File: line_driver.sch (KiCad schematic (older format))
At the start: 30 parts, among them J7 DRV632

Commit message: Add LEDs to MCU and polarized caps on line driver.
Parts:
- removed C12, C16, C19, C8: 1uF, symbol C
- added C12, C16, C19, C8: 1uF, symbol CP
- renumbered R7 to R10, R8 to R11, R9 to R12, R10 to R13, R11 to R14, R12 to R15, R13 to R16, R14 to R17, R15 to R18, R16 to R19, R17 to R20, R4 to R7, R5 to R8, R6 to R9
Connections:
- net L+: now also C19.1
- net L-: now also C16.1
- net R+: now also C12.1
- net R-: now also C8.1
- net at R15.1: now also C16.2
- net at R11.1: now also C12.2
- net at R17.1: now also C19.2
- net at R9.1: now also C8.2
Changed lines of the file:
@@
 $EndDescr
 $Comp
-L GND #PWR023
+L GND #PWR25
 U 1 1 59178E76
 P 4800 3400
-F 0 "#PWR023" H 4800 3150 50  0001 C CNN
+F 0 "#PWR25" H 4800 3150 50  0001 C CNN
 F 1 "GND" H 4800 3250 50  0000 C CNN
 F 2 "" H 4800 3400 50  0001 C CNN
@@
 $EndComp
 $Comp
-L GND #PWR024
+L GND #PWR31
 U 1 1 59178E8C
 P 6800 3500
-F 0 "#PWR024" H 6800 3250 50  0001 C CNN
+F 0 "#PWR31" H 6800 3250 50  0001 C CNN
 F 1 "GND" H 6800 3350 50  0000 C CNN
 F 2 "" H 6800 3500 50  0001 C CNN
@@
 $EndComp
 $Comp
-L GND #PWR025
+L GND #PWR27
 U 1 1 59178F5E
 P 5150 4050
-F 0 "#PWR025" H 5150 3800 50  0001 C CNN
+F 0 "#PWR27" H 5150 3800 50  0001 C CNN
 F 1 "GND" H 5150 3900 50  0000 C CNN
 F 2 "" H 5150 4050 50  0001 C CNN
@@
 $EndComp
 $Comp
-L GND #PWR026
+L GND #PWR29
 U 1 1 59178FEA
 P 6450 4050
-F 0 "#PWR026" H 6450 3800 50  0001 C CNN
+F 0 "#PWR29" H 6450 3800 50  0001 C CNN
 F 1 "GND" H 6450 3900 50  0000 C CNN
 F 2 "" H 6450 4050 50  0001 C CNN
@@
 	6450 3950 6450 4050
 $Comp
-L VCC #PWR027
+L VCC #PWR30
 U 1 1 59179027
 P 6650 3650
-F 0 "#PWR027" H 6650 3500 50  0001 C CNN
+F 0 "#PWR30" H 6650 3500 50  0001 C CNN
 F 1 "VCC" H 6650 3800 50  0000 C CNN
 F 2 "" H 6650 3650 50  0001 C CNN
@@
 Connection ~ 6450 3600
 $Comp
-L VCC #PWR028
+L VCC #PWR26
 U 1 1 59179085
 P 4950 3500
-F 0 "#PWR028" H 4950 3350 50  0001 C CNN
+F 0 "#PWR26" H 4950 3350 50  0001 C CNN
 F 1 "VCC" H 4950 3650 50  0000 C CNN
 F 2 "" H 4950 3500 50  0001 C CNN
@@
 $EndComp
 $Comp
-L R R10
+L R R13
 U 1 1 59179216
 P 5550 2350
-F 0 "R10" V 5630 2350 50  0000 C CNN
+F 0 "R13" V 5630 2350 50  0000 C CNN
 F 1 "30k" V 5550 2350 50  0000 C CNN
 F 2 "Resistors_THT:R_Axial_DIN0204_L3.6mm_D1.6mm_P1.90mm_Vertical" V 5480 2350 50  0001 C CNN
@@
 $EndComp
 $Comp
-L R R11
+L R R14
 U 1 1 59179241
 P 6050 2350
-F 0 "R11" V 6130 2350 50  0000 C CNN
+F 0 "R14" V 6130 2350 50  0000 C CNN
 F 1 "30k" V 6050 2350 50  0000 C CNN
 F 2 "Resistors_THT:R_Axial_DIN0204_L3.6mm_D1.6mm_P1.90mm_Vertical" V 5980 2350 50  0001 C CNN
@@
 $EndComp
 $Comp
-L GND #PWR029
+L GND #PWR28
 U 1 1 5917926C
 P 5800 2100
-F 0 "#PWR029" H 5800 1850 50  0001 C CNN
+F 0 "#PWR28" H 5800 1850 50  0001 C CNN
 F 1 "GND" H 5800 1950 50  0000 C CNN
 F 2 "" H 5800 2100 50  0001 C CNN
@@
 Connection ~ 5800 2350
 $Comp
-L R R13
+L R R16
 U 1 1 59179384
 P 6300 2550
-F 0 "R13" V 6380 2550 50  0000 C CNN
+F 0 "R16" V 6380 2550 50  0000 C CNN
 F 1 "43k" V 6300 2550 50  0000 C CNN
 F 2 "Resistors_THT:R_Axial_DIN0204_L3.6mm_D1.6mm_P1.90mm_Vertical" V 6230 2550 50  0001 C CNN
@@
 $EndComp
 $Comp
-L R R9
+L R R12
 U 1 1 591793C1
 P 5300 2550
-F 0 "R9" V 5380 2550 50  0000 C CNN
+F 0 "R12" V 5380 2550 50  0000 C CNN
 F 1 "43k" V 5300 2550 50  0000 C CNN
 F 2 "Resistors_THT:R_Axial_DIN0204_L3.6mm_D1.6mm_P1.90mm_Vertical" V 5230 2550 50  0001 C CNN
@@
 	5300 2700 5300 3100
 $Comp
-L R R12
+L R R15
 U 1 1 5917A21C
 P 6300 2150
-F 0 "R12" V 6380 2150 50  0000 C CNN
+F 0 "R15" V 6380 2150 50  0000 C CNN
 F 1 "15k" V 6300 2150 50  0000 C CNN
 F 2 "Resistors_THT:R_Axial_DIN0204_L3.6mm_D1.6mm_P1.90mm_Vertical" V 6230 2150 50  0001 C CNN
@@
 $EndComp
 $Comp
-L R R8
+L R R11
 U 1 1 5917A253
 P 5300 2150
-F 0 "R8" V 5380 2150 50  0000 C CNN
+F 0 "R11" V 5380 2150 50  0000 C CNN
 F 1 "15k" V 5300 2150 50  0000 C CNN
 F 2 "Resistors_THT:R_Axial_DIN0204_L3.6mm_D1.6mm_P1.90mm_Vertical" V 5230 2150 50  0001 C CNN
@@
 	6200 2350 6400 2350
 Connection ~ 6300 2350
-$Comp
-L C C16
-U 1 1 5917A3EF
-P 6300 1800
-F 0 "C16" H 6325 1900 50  0000 L CNN
-F 1 "1uF" H 6325 1700 50  0000 L CNN
-F 2 "" H 6338 1650 50  0001 C CNN
-F 3 "" H 6300 1800 50  0001 C CNN
-	1    6300 1800
-	1    0    0    -1
-$EndComp
-$Comp
-L C C12
-U 1 1 5917A42E
-P 5300 1800
-F 0 "C12" H 5325 1900 50  0000 L CNN
-F 1 "1uF" H 5325 1700 50  0000 L CNN
-F 2 "" H 5338 1650 50  0001 C CNN
-F 3 "" H 5300 1800 50  0001 C CNN
-	1    5300 1800
-	1    0    0    -1
-$EndComp
 Wire Wire Line
 	6300 1950 6300 2000
 Wire Wire Line
 	5300 1950 5300 2000
-$Comp
-L C C19
-U 1 1 5917A4E1
-P 6800 1800
-F 0 "C19" H 6825 1900 50  0000 L CNN
-F 1 "1uF" H 6825 1700 50  0000 L CNN
-F 2 "" H 6838 1650 50  0001 C CNN
-F 3 "" H 6800 1800 50  0001 C CNN
-	1    6800 1800
-	1    0    0    -1
-$EndComp
-$Comp
-L C C8
-U 1 1 5917A52C
-P 4800 1800
-F 0 "C8" H 4825 1900 50  0000 L CNN
-F 1 "1uF" H 4825 1700 50  0000 L CNN
-F 2 "" H 4838 1650 50  0001 C CNN
-F 3 "" H 4800 1800 50  0001 C CNN
-	1    4800 1800
-	1    0    0    -1
-$EndComp
 $Comp
 L C C10
@@
 	6700 2350 7050 2350
 $Comp
-L R R15
+L R R18
 U 1 1 5917A8A8
 P 6800 2550
-F 0 "R15" V 6880 2550 50  0000 C CNN
+F 0 "R18" V 6880 2550 50  0000 C CNN
 F 1 "43k" V 6800 2550 50  0000 C CNN
 F 2 "Resistors_THT:R_Axial_DIN0204_L3.6mm_D1.6mm_P1.90mm_Vertical" V 6730 2550 50  0001 C CNN
@@
 $EndComp
 $Comp
-L R R7
+L R R10
 U 1 1 5917A8FF
 P 4800 2550
-F 0 "R7" V 4880 2550 50  0000 C CNN
+F 0 "R10" V 4880 2550 50  0000 C CNN
 F 1 "43k" V 4800 2550 50  0000 C CNN
 F 2 "Resistors_THT:R_Axial_DIN0204_L3.6mm_D1.6mm_P1.90mm_Vertical" V 4730 2550 50  0001 C CNN
@@
 Connection ~ 4800 2350
 $Comp
-L R R14
+L R R17
 U 1 1 5917AA6A
 P 6800 2150
-F 0 "R14" V 6880 2150 50  0000 C CNN
+F 0 "R17" V 6880 2150 50  0000 C CNN
 F 1 "15k" V 6800 2150 50  0000 C CNN
 F 2 "Resistors_THT:R_Axial_DIN0204_L3.6mm_D1.6mm_P1.90mm_Vertical" V 6730 2150 50  0001 C CNN
@@
 $EndComp
 $Comp
-L R R6
+L R R9
 U 1 1 5917AAD3
 P 4800 2150
-F 0 "R6" V 4880 2150 50  0000 C CNN
+F 0 "R9" V 4880 2150 50  0000 C CNN
 F 1 "15k" V 4800 2150 50  0000 C CNN
 F 2 "Resistors_THT:R_Axial_DIN0204_L3.6mm_D1.6mm_P1.90mm_Vertical" V 4730 2150 50  0001 C CNN
@@
 Connection ~ 4800 2950
 $Comp
-L R R16
+L R R19
 U 1 1 5917AD17
 P 7050 2550
-F 0 "R16" V 7130 2550 50  0000 C CNN
+F 0 "R19" V 7130 2550 50  0000 C CNN
 F 1 "30k" V 7050 2550 50  0000 C CNN
 F 2 "Resistors_THT:R_Axial_DIN0204_L3.6mm_D1.6mm_P1.90mm_Vertical" V 6980 2550 50  0001 C CNN
@@
 $EndComp
 $Comp
-L R R5
+L R R8
 U 1 1 5917AD78
 P 4550 2550
-F 0 "R5" V 4630 2550 50  0000 C CNN
+F 0 "R8" V 4630 2550 50  0000 C CNN
 F 1 "30k" V 4550 2550 50  0000 C CNN
 F 2 "Resistors_THT:R_Axial_DIN0204_L3.6mm_D1.6mm_P1.90mm_Vertical" V 4480 2550 50  0001 C CNN
@@
 $EndComp
 $Comp
-L R R17
+L R R20
 U 1 1 59339334
 P 7250 3300
-F 0 "R17" V 7330 3300 50  0000 C CNN
+F 0 "R20" V 7330 3300 50  0000 C CNN
 F 1 "33" V 7250 3300 50  0000 C CNN
 F 2 "" V 7180 3300 50  0001 C CNN
@@
 $EndComp
 $Comp
-L R R4
+L R R7
 U 1 1 593393C3
 P 4350 3300
-F 0 "R4" V 4430 3300 50  0000 C CNN
+F 0 "R7" V 4430 3300 50  0000 C CNN
 F 1 "33" V 4350 3300 50  0000 C CNN
 F 2 "" V 4280 3300 50  0001 C CNN
@@
 Connection ~ 4100 3300
 $Comp
-L GND #PWR030
+L GND #PWR32
 U 1 1 59339996
 P 7500 3650
-F 0 "#PWR030" H 7500 3400 50  0001 C CNN
+F 0 "#PWR32" H 7500 3400 50  0001 C CNN
 F 1 "GND" H 7500 3500 50  0000 C CNN
 F 2 "" H 7500 3650 50  0001 C CNN
@@
 $EndComp
 $Comp
-L GND #PWR031
+L GND #PWR24
 U 1 1 593399E6
 P 4100 3650
-F 0 "#PWR031" H 4100 3400 50  0001 C CNN
+F 0 "#PWR24" H 4100 3400 50  0001 C CNN
 F 1 "GND" H 4100 3500 50  0000 C CNN
 F 2 "" H 4100 3650 50  0001 C CNN
@@
 Wire Wire Line
 	4100 3600 4100 3650
+$Comp
+L CP C8
+U 1 1 5939D955
+P 4800 1800
+F 0 "C8" H 4825 1900 50  0000 L CNN
+F 1 "1uF" H 4825 1700 50  0000 L CNN
+F 2 "" H 4838 1650 50  0001 C CNN
+F 3 "" H 4800 1800 50  0001 C CNN
+	1    4800 1800
+	1    0    0    -1
+$EndComp
+$Comp
+L CP C12
+U 1 1 5939DA1E
+P 5300 1800
+F 0 "C12" H 5325 1900 50  0000 L CNN
+F 1 "1uF" H 5325 1700 50  0000 L CNN
+F 2 "" H 5338 1650 50  0001 C CNN
+F 3 "" H 5300 1800 50  0001 C CNN
+	1    5300 1800
+	1    0    0    -1
+$EndComp
+$Comp
+L CP C16
+U 1 1 5939DA7F
+P 6300 1800
+F 0 "C16" H 6325 1900 50  0000 L CNN
+F 1 "1uF" H 6325 1700 50  0000 L CNN
+F 2 "" H 6338 1650 50  0001 C CNN
+F 3 "" H 6300 1800 50  0001 C CNN
+	1    6300 1800
+	1    0    0    -1
+$EndComp
+$Comp
+L CP C19
+U 1 1 5939DADA
+P 6800 1800
+F 0 "C19" H 6825 1900 50  0000 L CNN
+F 1 "1uF" H 6825 1700 50  0000 L CNN
+F 2 "" H 6838 1650 50  0001 C CNN
+F 3 "" H 6800 1800 50  0001 C CNN
+	1    6800 1800
+	1    0    0    -1
+$EndComp
 $EndSCHEMATC

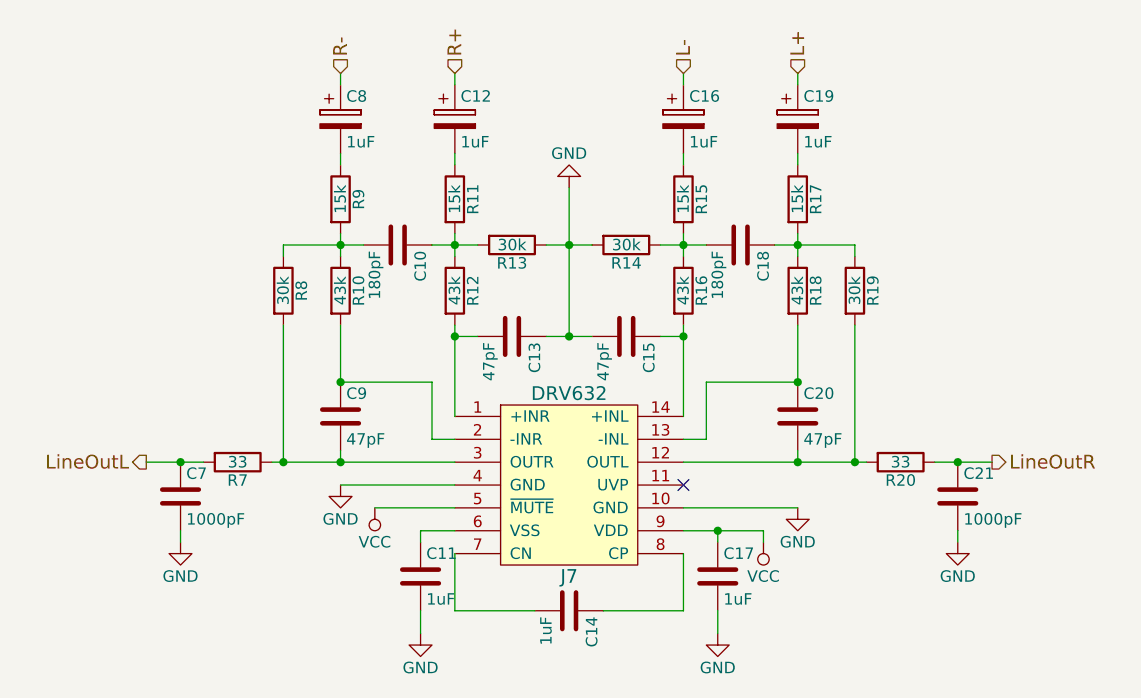
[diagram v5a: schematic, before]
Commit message: Add resistor values to LEDs and a voltage regulator. Has power pin errors still.
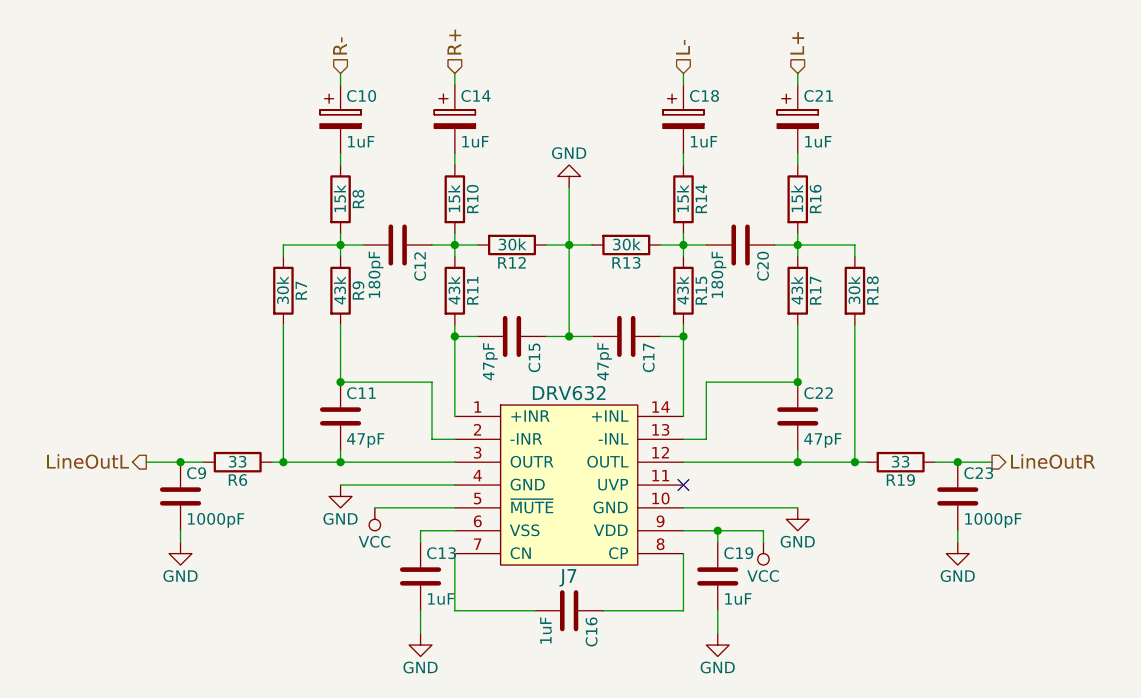
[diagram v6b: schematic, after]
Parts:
- renumbered C8 to C10, C9 to C11, C10 to C12, C11 to C13, C12 to C14, C13 to C15, C14 to C16, C15 to C17, C16 to C18, C17 to C19, C18 to C20, C19 to C21, C20 to C22, C21 to C23, C7 to C9, R11 to R10, R12 to R11, R13 to R12, R14 to R13, R15 to R14, R16 to R15, R17 to R16, R18 to R17, R19 to R18, R20 to R19, R7 to R6, R8 to R7, R9 to R8, R10 to R9
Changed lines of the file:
@@
 $EndDescr
 $Comp
-L GND #PWR25
+L GND #PWR028
 U 1 1 59178E76
 P 4800 3400
-F 0 "#PWR25" H 4800 3150 50  0001 C CNN
+F 0 "#PWR028" H 4800 3150 50  0001 C CNN
 F 1 "GND" H 4800 3250 50  0000 C CNN
 F 2 "" H 4800 3400 50  0001 C CNN
@@
 $EndComp
 $Comp
-L GND #PWR31
+L GND #PWR029
 U 1 1 59178E8C
 P 6800 3500
-F 0 "#PWR31" H 6800 3250 50  0001 C CNN
+F 0 "#PWR029" H 6800 3250 50  0001 C CNN
 F 1 "GND" H 6800 3350 50  0000 C CNN
 F 2 "" H 6800 3500 50  0001 C CNN
@@
 $EndComp
 $Comp
-L C C14
+L C C16
 U 1 1 59178EA2
 P 5800 3950
-F 0 "C14" H 5825 4050 50  0000 L CNN
+F 0 "C16" H 5825 4050 50  0000 L CNN
 F 1 "1uF" H 5825 3850 50  0000 L CNN
 F 2 "" H 5838 3800 50  0001 C CNN
@@
 	6300 3500 6800 3500
 $Comp
-L C C11
+L C C13
 U 1 1 59178EFD
 P 5150 3800
-F 0 "C11" H 5175 3900 50  0000 L CNN
+F 0 "C13" H 5175 3900 50  0000 L CNN
 F 1 "1uF" H 5175 3700 50  0000 L CNN
 F 2 "" H 5188 3650 50  0001 C CNN
@@
 $EndComp
 $Comp
-L GND #PWR27
+L GND #PWR030
 U 1 1 59178F5E
 P 5150 4050
-F 0 "#PWR27" H 5150 3800 50  0001 C CNN
+F 0 "#PWR030" H 5150 3800 50  0001 C CNN
 F 1 "GND" H 5150 3900 50  0000 C CNN
 F 2 "" H 5150 4050 50  0001 C CNN
@@
 	5150 3950 5150 4050
 $Comp
-L C C17
+L C C19
 U 1 1 59178FC9
 P 6450 3800
-F 0 "C17" H 6475 3900 50  0000 L CNN
+F 0 "C19" H 6475 3900 50  0000 L CNN
 F 1 "1uF" H 6475 3700 50  0000 L CNN
 F 2 "" H 6488 3650 50  0001 C CNN
@@
 $EndComp
 $Comp
-L GND #PWR29
+L GND #PWR031
 U 1 1 59178FEA
 P 6450 4050
-F 0 "#PWR29" H 6450 3800 50  0001 C CNN
+F 0 "#PWR031" H 6450 3800 50  0001 C CNN
 F 1 "GND" H 6450 3900 50  0000 C CNN
 F 2 "" H 6450 4050 50  0001 C CNN
@@
 	6450 3950 6450 4050
 $Comp
-L VCC #PWR30
+L VCC #PWR032
 U 1 1 59179027
 P 6650 3650
-F 0 "#PWR30" H 6650 3500 50  0001 C CNN
+F 0 "#PWR032" H 6650 3500 50  0001 C CNN
 F 1 "VCC" H 6650 3800 50  0000 C CNN
 F 2 "" H 6650 3650 50  0001 C CNN
@@
 Connection ~ 6450 3600
 $Comp
-L VCC #PWR26
+L VCC #PWR033
 U 1 1 59179085
 P 4950 3500
-F 0 "#PWR26" H 4950 3350 50  0001 C CNN
+F 0 "#PWR033" H 4950 3350 50  0001 C CNN
 F 1 "VCC" H 4950 3650 50  0000 C CNN
 F 2 "" H 4950 3500 50  0001 C CNN
@@
 LineOutL
 $Comp
-L C C20
+L C C22
 U 1 1 59179109
 P 6800 3100
-F 0 "C20" H 6825 3200 50  0000 L CNN
+F 0 "C22" H 6825 3200 50  0000 L CNN
 F 1 "47pF" H 6825 3000 50  0000 L CNN
 F 2 "" H 6838 2950 50  0001 C CNN
@@
 $EndComp
 $Comp
-L C C9
+L C C11
 U 1 1 5917915A
 P 4800 3100
-F 0 "C9" H 4825 3200 50  0000 L CNN
+F 0 "C11" H 4825 3200 50  0000 L CNN
 F 1 "47pF" H 4825 3000 50  0000 L CNN
 F 2 "" H 4838 2950 50  0001 C CNN
@@
 	6400 3200 6300 3200
 $Comp
-L C C15
+L C C17
 U 1 1 591791B6
 P 6050 2750
-F 0 "C15" H 6075 2850 50  0000 L CNN
+F 0 "C17" H 6075 2850 50  0000 L CNN
 F 1 "47pF" H 6075 2650 50  0000 L CNN
 F 2 "" H 6088 2600 50  0001 C CNN
@@
 $EndComp
 $Comp
-L C C13
+L C C15
 U 1 1 591791EB
 P 5550 2750
-F 0 "C13" H 5575 2850 50  0000 L CNN
+F 0 "C15" H 5575 2850 50  0000 L CNN
 F 1 "47pF" H 5575 2650 50  0000 L CNN
 F 2 "" H 5588 2600 50  0001 C CNN
@@
 $EndComp
 $Comp
-L R R13
+L R R12
 U 1 1 59179216
 P 5550 2350
-F 0 "R13" V 5630 2350 50  0000 C CNN
+F 0 "R12" V 5630 2350 50  0000 C CNN
 F 1 "30k" V 5550 2350 50  0000 C CNN
 F 2 "Resistors_THT:R_Axial_DIN0204_L3.6mm_D1.6mm_P1.90mm_Vertical" V 5480 2350 50  0001 C CNN
@@
 $EndComp
 $Comp
-L R R14
+L R R13
 U 1 1 59179241
 P 6050 2350
-F 0 "R14" V 6130 2350 50  0000 C CNN
+F 0 "R13" V 6130 2350 50  0000 C CNN
 F 1 "30k" V 6050 2350 50  0000 C CNN
 F 2 "Resistors_THT:R_Axial_DIN0204_L3.6mm_D1.6mm_P1.90mm_Vertical" V 5980 2350 50  0001 C CNN
@@
 $EndComp
 $Comp
-L GND #PWR28
+L GND #PWR034
 U 1 1 5917926C
 P 5800 2100
-F 0 "#PWR28" H 5800 1850 50  0001 C CNN
+F 0 "#PWR034" H 5800 1850 50  0001 C CNN
 F 1 "GND" H 5800 1950 50  0000 C CNN
 F 2 "" H 5800 2100 50  0001 C CNN
@@
 Connection ~ 5800 2350
 $Comp
-L R R16
+L R R15
 U 1 1 59179384
 P 6300 2550
-F 0 "R16" V 6380 2550 50  0000 C CNN
+F 0 "R15" V 6380 2550 50  0000 C CNN
 F 1 "43k" V 6300 2550 50  0000 C CNN
 F 2 "Resistors_THT:R_Axial_DIN0204_L3.6mm_D1.6mm_P1.90mm_Vertical" V 6230 2550 50  0001 C CNN
@@
 $EndComp
 $Comp
-L R R12
+L R R11
 U 1 1 591793C1
 P 5300 2550
-F 0 "R12" V 5380 2550 50  0000 C CNN
+F 0 "R11" V 5380 2550 50  0000 C CNN
 F 1 "43k" V 5300 2550 50  0000 C CNN
 F 2 "Resistors_THT:R_Axial_DIN0204_L3.6mm_D1.6mm_P1.90mm_Vertical" V 5230 2550 50  0001 C CNN
@@
 	5300 2700 5300 3100
 $Comp
-L R R15
+L R R14
 U 1 1 5917A21C
 P 6300 2150
-F 0 "R15" V 6380 2150 50  0000 C CNN
+F 0 "R14" V 6380 2150 50  0000 C CNN
 F 1 "15k" V 6300 2150 50  0000 C CNN
 F 2 "Resistors_THT:R_Axial_DIN0204_L3.6mm_D1.6mm_P1.90mm_Vertical" V 6230 2150 50  0001 C CNN
@@
 $EndComp
 $Comp
-L R R11
+L R R10
 U 1 1 5917A253
 P 5300 2150
-F 0 "R11" V 5380 2150 50  0000 C CNN
+F 0 "R10" V 5380 2150 50  0000 C CNN
 F 1 "15k" V 5300 2150 50  0000 C CNN
 F 2 "Resistors_THT:R_Axial_DIN0204_L3.6mm_D1.6mm_P1.90mm_Vertical" V 5230 2150 50  0001 C CNN
@@
 	5300 1950 5300 2000
 $Comp
-L C C10
+L C C12
 U 1 1 5917A56B
 P 5050 2350
-F 0 "C10" H 5075 2450 50  0000 L CNN
+F 0 "C12" H 5075 2450 50  0000 L CNN
 F 1 "180pF" H 5075 2250 50  0000 L CNN
 F 2 "" H 5088 2200 50  0001 C CNN
@@
 $EndComp
 $Comp
-L C C18
+L C C20
 U 1 1 5917A5AC
 P 6550 2350
-F 0 "C18" H 6575 2450 50  0000 L CNN
+F 0 "C20" H 6575 2450 50  0000 L CNN
 F 1 "180pF" H 6575 2250 50  0000 L CNN
 F 2 "" H 6588 2200 50  0001 C CNN
@@
 	6700 2350 7050 2350
 $Comp
-L R R18
+L R R17
 U 1 1 5917A8A8
 P 6800 2550
-F 0 "R18" V 6880 2550 50  0000 C CNN
+F 0 "R17" V 6880 2550 50  0000 C CNN
 F 1 "43k" V 6800 2550 50  0000 C CNN
 F 2 "Resistors_THT:R_Axial_DIN0204_L3.6mm_D1.6mm_P1.90mm_Vertical" V 6730 2550 50  0001 C CNN
@@
 $EndComp
 $Comp
-L R R10
+L R R9
 U 1 1 5917A8FF
 P 4800 2550
-F 0 "R10" V 4880 2550 50  0000 C CNN
+F 0 "R9" V 4880 2550 50  0000 C CNN
 F 1 "43k" V 4800 2550 50  0000 C CNN
 F 2 "Resistors_THT:R_Axial_DIN0204_L3.6mm_D1.6mm_P1.90mm_Vertical" V 4730 2550 50  0001 C CNN
@@
 Connection ~ 4800 2350
 $Comp
-L R R17
+L R R16
 U 1 1 5917AA6A
 P 6800 2150
-F 0 "R17" V 6880 2150 50  0000 C CNN
+F 0 "R16" V 6880 2150 50  0000 C CNN
 F 1 "15k" V 6800 2150 50  0000 C CNN
 F 2 "Resistors_THT:R_Axial_DIN0204_L3.6mm_D1.6mm_P1.90mm_Vertical" V 6730 2150 50  0001 C CNN
@@
 $EndComp
 $Comp
-L R R9
+L R R8
 U 1 1 5917AAD3
 P 4800 2150
-F 0 "R9" V 4880 2150 50  0000 C CNN
+F 0 "R8" V 4880 2150 50  0000 C CNN
 F 1 "15k" V 4800 2150 50  0000 C CNN
 F 2 "Resistors_THT:R_Axial_DIN0204_L3.6mm_D1.6mm_P1.90mm_Vertical" V 4730 2150 50  0001 C CNN
@@
 Connection ~ 4800 2950
 $Comp
-L R R19
+L R R18
 U 1 1 5917AD17
 P 7050 2550
-F 0 "R19" V 7130 2550 50  0000 C CNN
+F 0 "R18" V 7130 2550 50  0000 C CNN
 F 1 "30k" V 7050 2550 50  0000 C CNN
 F 2 "Resistors_THT:R_Axial_DIN0204_L3.6mm_D1.6mm_P1.90mm_Vertical" V 6980 2550 50  0001 C CNN
@@
 $EndComp
 $Comp
-L R R8
+L R R7
 U 1 1 5917AD78
 P 4550 2550
-F 0 "R8" V 4630 2550 50  0000 C CNN
+F 0 "R7" V 4630 2550 50  0000 C CNN
 F 1 "30k" V 4550 2550 50  0000 C CNN
 F 2 "Resistors_THT:R_Axial_DIN0204_L3.6mm_D1.6mm_P1.90mm_Vertical" V 4480 2550 50  0001 C CNN
@@
 $EndComp
 $Comp
-L C C21
+L C C23
 U 1 1 5933924A
 P 7500 3450
-F 0 "C21" H 7525 3550 50  0000 L CNN
+F 0 "C23" H 7525 3550 50  0000 L CNN
 F 1 "1000pF" H 7525 3350 50  0000 L CNN
 F 2 "" H 7538 3300 50  0001 C CNN
@@
 $EndComp
 $Comp
-L C C7
+L C C9
 U 1 1 593392DF
 P 4100 3450
-F 0 "C7" H 4125 3550 50  0000 L CNN
+F 0 "C9" H 4125 3550 50  0000 L CNN
 F 1 "1000pF" H 4125 3350 50  0000 L CNN
 F 2 "" H 4138 3300 50  0001 C CNN
@@
 $EndComp
 $Comp
-L R R20
+L R R19
 U 1 1 59339334
 P 7250 3300
-F 0 "R20" V 7330 3300 50  0000 C CNN
+F 0 "R19" V 7330 3300 50  0000 C CNN
 F 1 "33" V 7250 3300 50  0000 C CNN
 F 2 "" V 7180 3300 50  0001 C CNN
@@
 $EndComp
 $Comp
-L R R7
+L R R6
 U 1 1 593393C3
 P 4350 3300
-F 0 "R7" V 4430 3300 50  0000 C CNN
+F 0 "R6" V 4430 3300 50  0000 C CNN
 F 1 "33" V 4350 3300 50  0000 C CNN
 F 2 "" V 4280 3300 50  0001 C CNN
@@
 Connection ~ 4100 3300
 $Comp
-L GND #PWR32
+L GND #PWR035
 U 1 1 59339996
 P 7500 3650
-F 0 "#PWR32" H 7500 3400 50  0001 C CNN
+F 0 "#PWR035" H 7500 3400 50  0001 C CNN
 F 1 "GND" H 7500 3500 50  0000 C CNN
 F 2 "" H 7500 3650 50  0001 C CNN
@@
 $EndComp
 $Comp
-L GND #PWR24
+L GND #PWR036
 U 1 1 593399E6
 P 4100 3650
-F 0 "#PWR24" H 4100 3400 50  0001 C CNN
+F 0 "#PWR036" H 4100 3400 50  0001 C CNN
 F 1 "GND" H 4100 3500 50  0000 C CNN
 F 2 "" H 4100 3650 50  0001 C CNN
@@
 	4100 3600 4100 3650
 $Comp
-L CP C8
+L CP C10
 U 1 1 5939D955
 P 4800 1800
-F 0 "C8" H 4825 1900 50  0000 L CNN
+F 0 "C10" H 4825 1900 50  0000 L CNN
 F 1 "1uF" H 4825 1700 50  0000 L CNN
 F 2 "" H 4838 1650 50  0001 C CNN
@@
 $EndComp
 $Comp
-L CP C12
+L CP C14
 U 1 1 5939DA1E
 P 5300 1800
-F 0 "C12" H 5325 1900 50  0000 L CNN
+F 0 "C14" H 5325 1900 50  0000 L CNN
 F 1 "1uF" H 5325 1700 50  0000 L CNN
 F 2 "" H 5338 1650 50  0001 C CNN
@@
 $EndComp
 $Comp
-L CP C16
+L CP C18
 U 1 1 5939DA7F
 P 6300 1800
-F 0 "C16" H 6325 1900 50  0000 L CNN
+F 0 "C18" H 6325 1900 50  0000 L CNN
 F 1 "1uF" H 6325 1700 50  0000 L CNN
 F 2 "" H 6338 1650 50  0001 C CNN
@@
 $EndComp
 $Comp
-L CP C19
+L CP C21
 U 1 1 5939DADA
 P 6800 1800
-F 0 "C19" H 6825 1900 50  0000 L CNN
+F 0 "C21" H 6825 1900 50  0000 L CNN
 F 1 "1uF" H 6825 1700 50  0000 L CNN
 F 2 "" H 6838 1650 50  0001 C CNN
